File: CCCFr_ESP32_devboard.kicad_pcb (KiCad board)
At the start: 4 copper layers, 54 x 85.6 mm, 215 parts, among them J1 USB_C_Receptacle_USB2.0_14P, J2 Conn_01x02_Pin, J3 Conn_01x18_Pin, J5 Conn_01x18_Pin, Q1 AO3401A, U1 ESP32-S3, U2 W25Q128JVS, U3 MCP73831-2-OT, U4 AMS1117-3.3, U5 TPS61023DRLR, Y1 32.768 kHz, Y2 40MHz(10ppm)

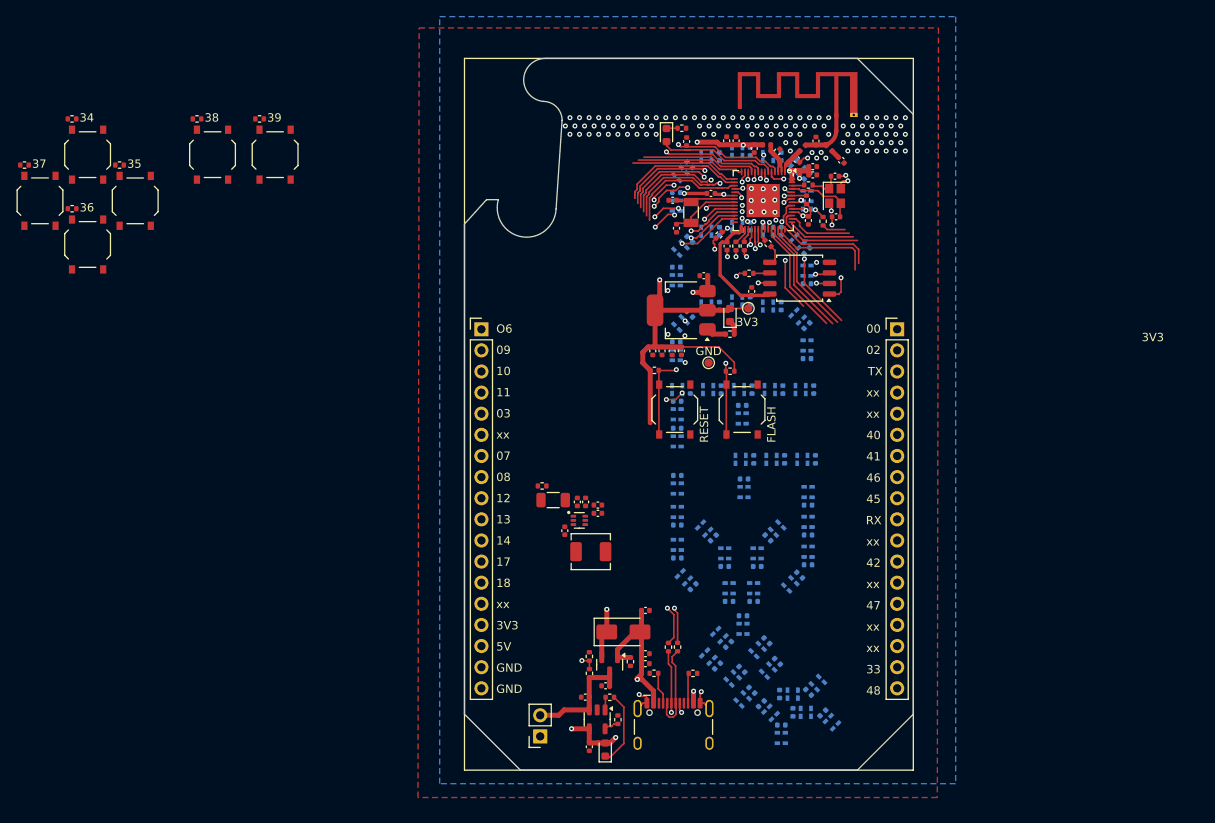
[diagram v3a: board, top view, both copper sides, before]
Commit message: rearrandged footprints
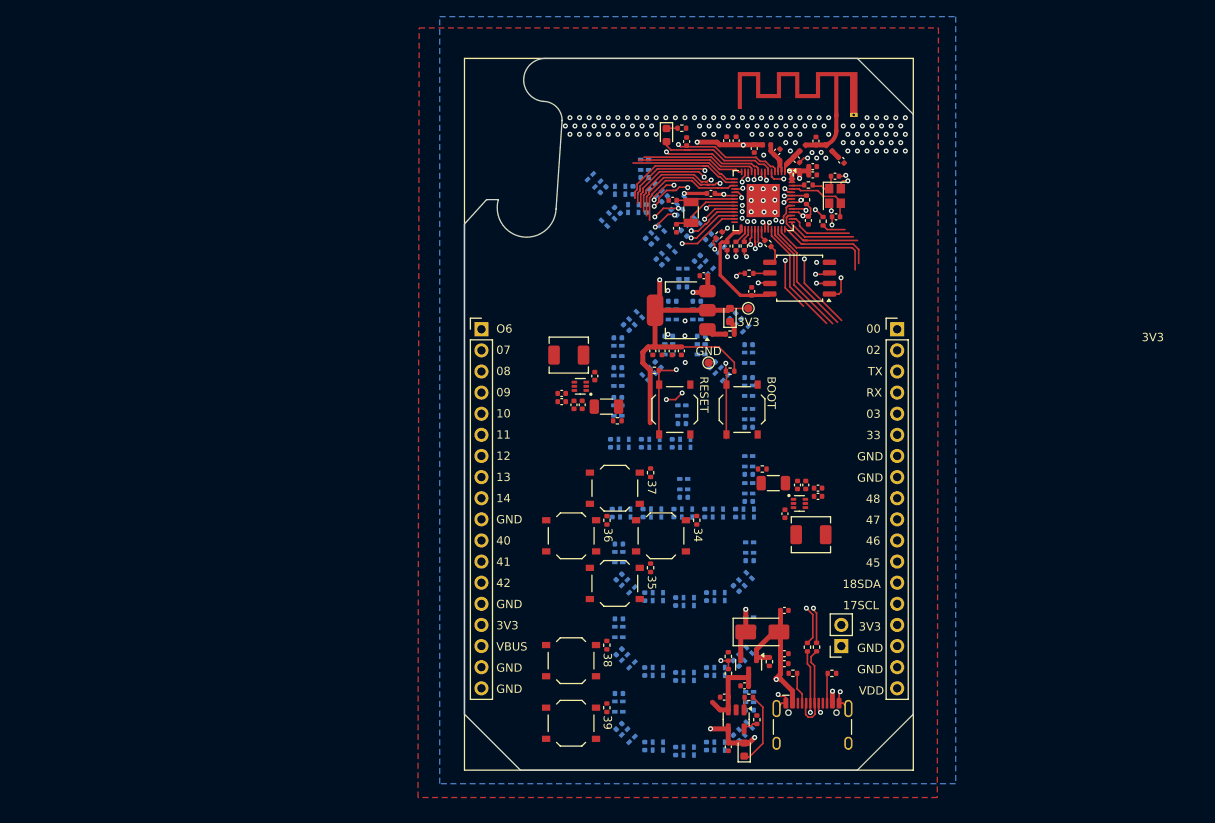
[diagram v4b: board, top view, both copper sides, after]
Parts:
- added C94: 10uF, Capacitor_SMD:C_0402_1005Metric, F.Cu at (147.9, 74.8)
- added C95: 10uF, Capacitor_SMD:C_0402_1005Metric, F.Cu at (143.9, 77.9)
- added C96: 10uF, Capacitor_SMD:C_0402_1005Metric, F.Cu at (143.9, 76.9)
- added C97: 10uF, Capacitor_SMD:C_0402_1005Metric, F.Cu at (145.3, 78.2)
- added C98: 10uF, Capacitor_SMD:C_0402_1005Metric, F.Cu at (146.3, 78.2)
- added L2: 1uH, Inductor_SMD:L_TechFuse_SL0420, F.Cu at (144.7, 72.2)
- added R11: 100K, Resistor_SMD:R_0402_1005Metric, F.Cu at (150.6, 80.2)
- added R13: 732K, Resistor_SMD:R_1206_3216Metric, F.Cu at (149.3, 78.5)
- added U6: TPS61023DRLR, PCM_SparkFun-Semiconductor-Standard:SOT-563, F.Cu at (146.1, 76.0)
- moved R5 89.3 mm to (160.1, 92.1), turned to 90 degrees
- moved R6 83.9 mm to (154.6, 86.4), turned to 90 degrees
- moved BTN3 82.8 mm to (155.8, 94.0), turned to 180 degrees
- moved R9 82.2 mm to (149.3, 114.7), turned to 90 degrees
- moved R8 80.2 mm to (149.3, 107.1), turned to 90 degrees
- moved R3 80.2 mm to (154.6, 97.8), turned to 90 degrees
- moved BTN4 77.3 mm to (150.3, 88.3), turned to 180 degrees
- moved BTN7 77.1 mm to (145.0, 116.5), turned to 180 degrees
- moved BTN6 74.6 mm to (145.0, 109.0), turned to 180 degrees
- moved R7 74.4 mm to (149.3, 92.1), turned to 90 degrees
- moved BTN2 73.8 mm to (150.3, 99.7), turned to 180 degrees
- moved C9 72.8 mm to (153.9, 119.3), turned to -90 degrees
- moved C5 72.7 mm to (157.6, 119.9), turned to -90 degrees
- moved D6 72.3 mm to (159.2, 119.9), turned to 180 degrees
- moved D7 72.1 mm to (155.4, 119.3), turned to 180 degrees
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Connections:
- J3 pad 10: IO13 -> GND
- J3 pad 11: IO14 -> IO40
- J3 pad 12: IO17/SCL -> IO41
- J3 pad 13: IO18/SDA -> IO42
- J3 pad 14: unconnected-(J3-Pin_14-Pad14) -> GND
- J3 pad 2: IO9 -> IO7
- J3 pad 3: IO10 -> IO8
- J3 pad 4: IO11 -> IO9
- J3 pad 5: IO3 -> IO10
- J3 pad 6: unconnected-(J3-Pin_6-Pad6) -> IO11
- J3 pad 7: IO7 -> IO12
- J3 pad 8: IO8 -> IO13
- J3 pad 9: IO12 -> IO14
- J5 pad 10: RX -> IO47
- J5 pad 11: unconnected-(J5-Pin_11-Pad11) -> IO46
- J5 pad 12: IO42 -> IO45
- J5 pad 13: unconnected-(J5-Pin_13-Pad13) -> IO18/SDA
- J5 pad 14: IO47 -> IO17/SCL
- J5 pad 15: unconnected-(J5-Pin_15-Pad15) -> VDD_CPU
- J5 pad 16: unconnected-(J5-Pin_16-Pad16) -> GND
- J5 pad 17: IO33 -> GND
- J5 pad 18: IO48 -> LED_VDD
- J5 pad 4: unconnected-(J5-Pin_4-Pad4) -> RX
- J5 pad 5: unconnected-(J5-Pin_5-Pad5) -> IO3
- J5 pad 6: IO40 -> IO33
- J5 pad 7: IO41 -> GND
- J5 pad 8: IO46 -> GND
- J5 pad 9: IO45 -> IO48
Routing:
- net VSYS: track 48.9 -> 11.8 mm
- net USB_D-: track 70.4 -> 37.0 mm
- net USB_D+: track 67.7 -> 34.4 mm
- net 5V: track 52.8 -> 36.8 mm
- net LED_VDD: track 0.00 -> 4.53 mm
- net IO0: track 25.2 -> 20.8 mm
- net VBAT: track 14.1 -> 10.2 mm
- net Net-(D60-DOUT): track 1.23 -> 0.00 mm
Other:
- board text added: "17SCL"
- board text added: "18SDA"
- board text added: "BOOT"
- board text added: "VBUS"
- board text added: "VDD"
- board text removed: "17"
- board text removed: "18"
- board text removed: "5V"
- board text removed: "FLASH"
- board text removed: "xx"

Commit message: Added JST plug for battery
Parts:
- added G***: LOGO, kustom:cccfr_silk_small, F.Cu at (156.0, 114.6)
- added J4: JST_2mm_LiPo, Connector_JST:JST_PH_B2B-PH-K_1x02_P2.00mm_Vertical, F.Cu at (174.1, 95.6)
- added Ref**: Val**, PCM_SparkFun-Aesthetic:OSHW_Logo_4mm, F.Cu at (155.6, 108.4)
- moved C89 15.2 mm to (172.8, 76.3)
- moved C92 15.2 mm to (176.8, 73.2)
- moved L1 15.2 mm to (175.9, 78.8)
- moved R4 15.2 mm to (170.1, 70.9)
- moved C90 15.2 mm to (174.3, 72.8)
- moved C91 15.2 mm to (175.3, 72.8)
- moved R10 15.2 mm to (171.4, 72.6)
- moved U5 15.2 mm to (174.5, 75.0)
- moved C93 15.2 mm to (176.8, 74.2)
- moved C1 1.83 mm to (161.7, 117.5)
- moved C21 1.83 mm to (151.2, 115.1)
- moved C23 1.83 mm to (166.9, 113.2)
- moved C28 1.83 mm to (158.0, 109.1)
- moved C47 1.83 mm to (151.2, 97.2)
- moved C48 1.83 mm to (166.9, 95.2)
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
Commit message: routed a bit
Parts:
- moved R17 1.15 mm to (175.5, 111.3), turned to -90 degrees
- moved J2 0.53 mm to (177.0, 107.2)
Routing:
- net VSYS: track 11.8 -> 109.8 mm, vias 2 -> 4
- net VDD_CPU: track 106.1 -> 182.5 mm, vias 7 -> 8
- net IO5: track 18.5 -> 78.7 mm, vias 2 -> 4
- net VBAT: track 10.2 -> 52.0 mm
- net IO4/BAT: track 40.6 -> 81.1 mm
- net 5V: track 36.8 -> 62.8 mm, vias 4 -> 5
- net GND: track 18.0 -> 41.6 mm, vias 129 -> 208
- net IO21: track 29.7 -> 7.53 mm, vias 3 -> 1
- net LED_VDD: track 4.53 -> 20.9 mm
- net Net-(U5-SW): track 0.00 -> 6.22 mm
- net Net-(U6-SW): track 0.00 -> 6.13 mm
- net Net-(U6-FB): track 0.00 -> 4.70 mm
- net Net-(U5-FB): track 0.00 -> 1.86 mm
- net Net-(J1-CC2): track 3.02 -> 2.43 mm
- net (no net): track 0.00 -> 0.50 mm, vias 0 -> 2
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- added copper zone on In1.Cu, net GND
- added copper zone on In2.Cu, net GND
- removed copper zone on B.Cu, net GND
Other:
- board text added: "+"

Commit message: added some instructions
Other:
- board text added: "ピン にじゅういち ライトテ プのデジタル入力 ピン ご ライトのオン オフスイッチ びんあけ は いちど しか つかえません"
